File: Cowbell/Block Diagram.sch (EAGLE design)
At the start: 0 parts

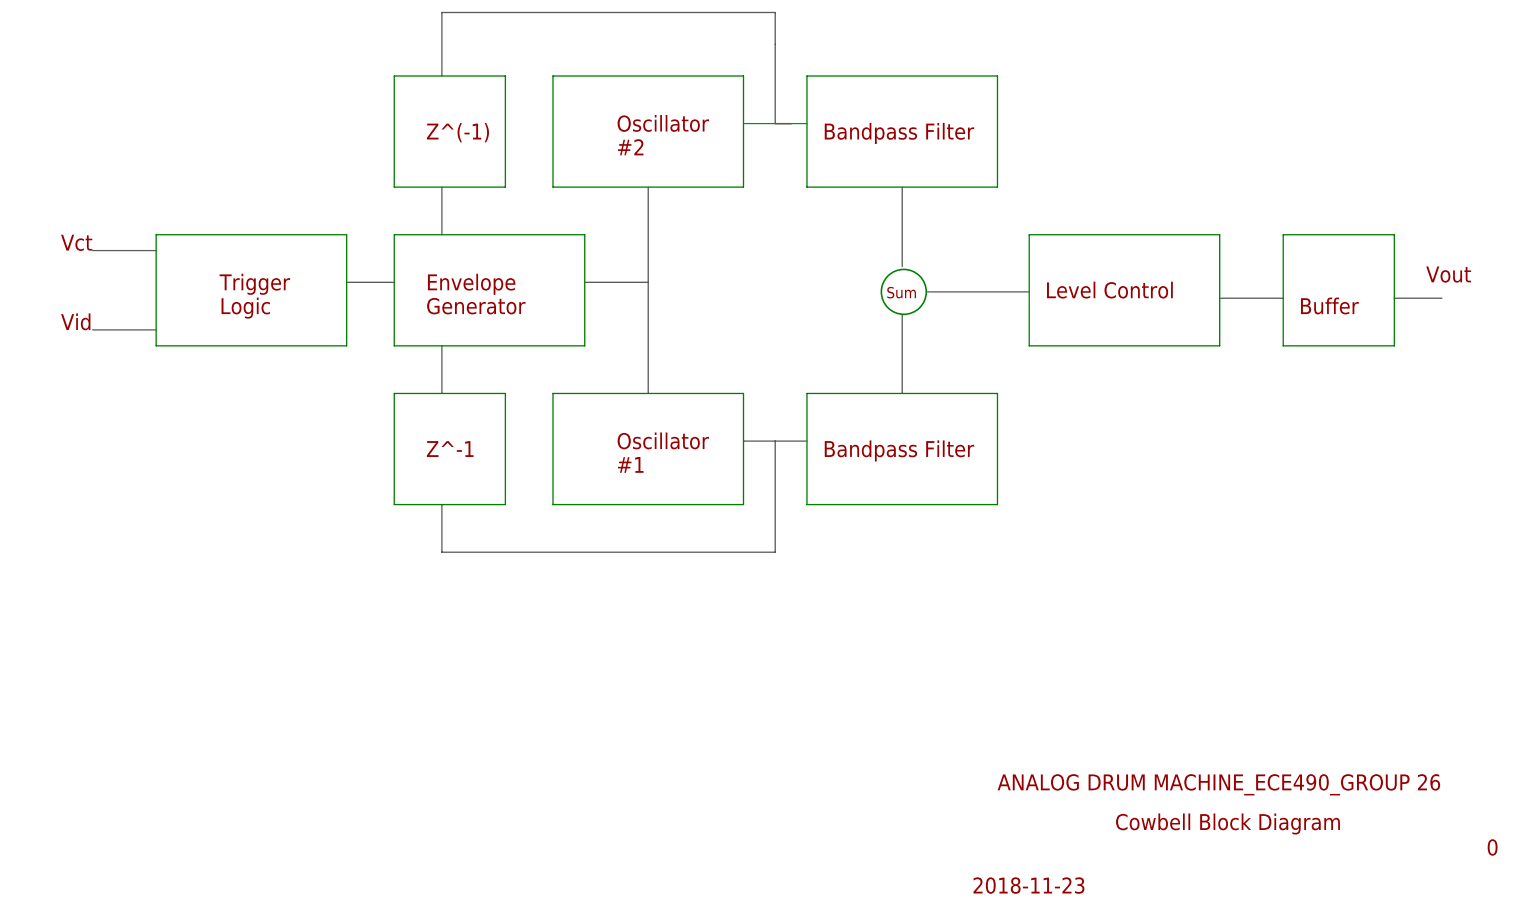
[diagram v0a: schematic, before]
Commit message: Added the Schmitt Triggers
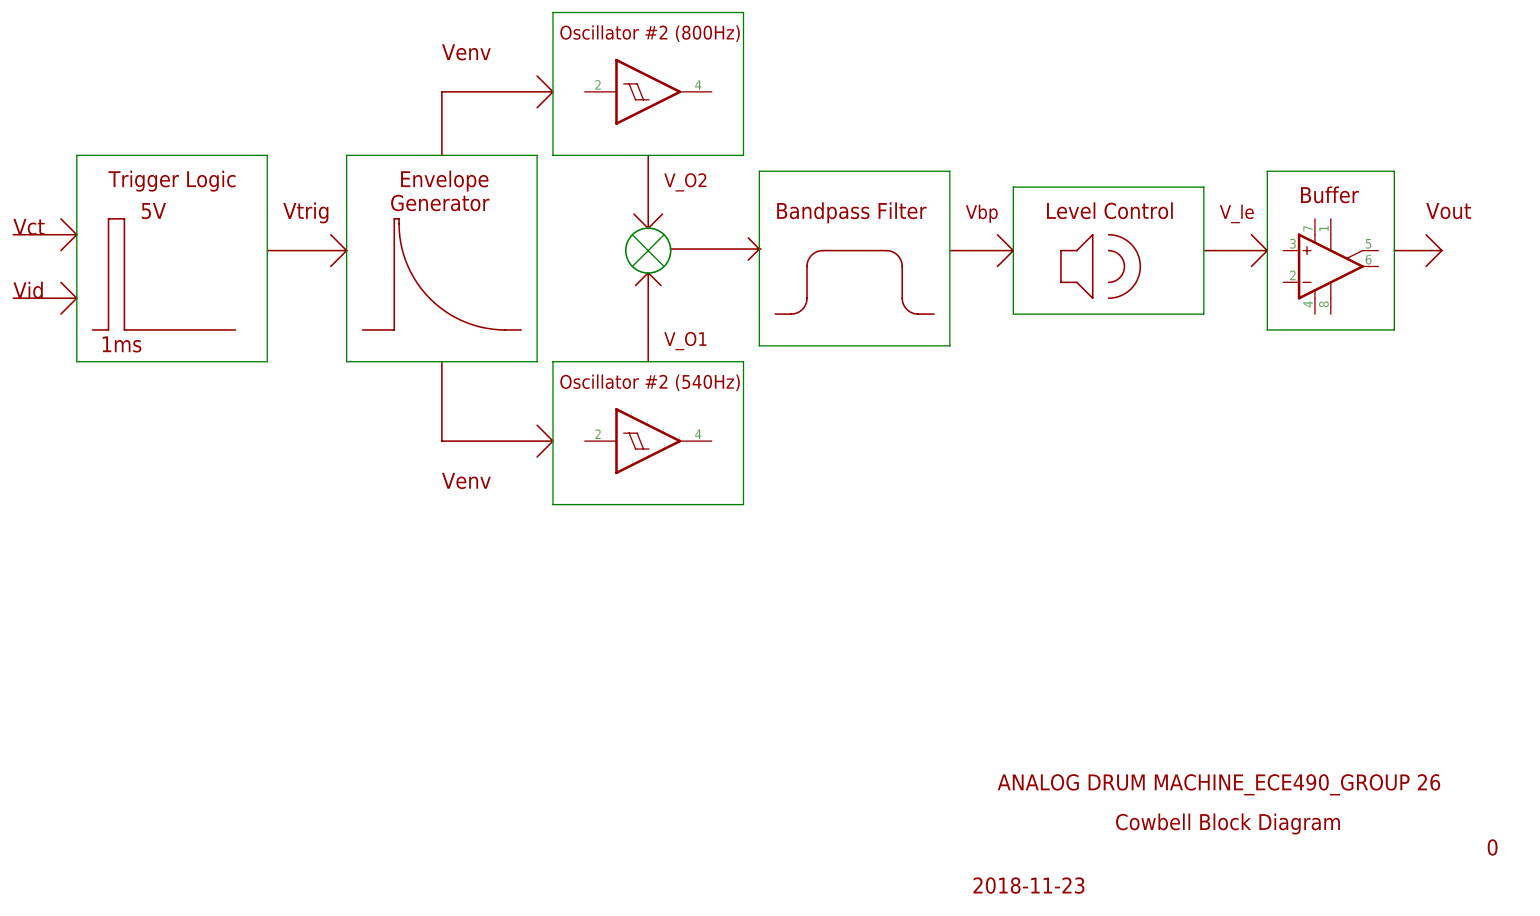
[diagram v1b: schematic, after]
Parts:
- added IC1, IC2: 74AUC1G17DBV, 74xx-little-us:74AUC1G17DBV
- added IC3: LM741D, linear:LM741D
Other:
- note added: "1ms"
- note added: "5V"
- note added: "Oscillator #2 (540Hz)"
- note added: "Oscillator #2 (800Hz)"
- note added: "V_O1"
- note added: "V_O2"
- note added: "V_le"
- note added: "Vbp"
- note added: "Venv"
- note added: "Vtrig"
- note removed: "Oscillator #1"
- note removed: "Oscillator #2"
- note removed: "Sum"
- note removed: "Z^(-1)"
- note removed: "Z^-1"
